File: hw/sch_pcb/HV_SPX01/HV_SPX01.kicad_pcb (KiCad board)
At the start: 2 copper layers, 21 x 23.1 mm, 37 parts, among them IC1 MAX1847EEE+, J1 Conn_01x01_Pin, J2 Conn_01x01_Pin, J3 Conn_01x01_Pin, J4 Conn_01x01_Pin, J5 Conn_01x01_Pin, J6 Conn_01x01_Pin, J7 Conn_01x01_Pin, Q1 PMOS

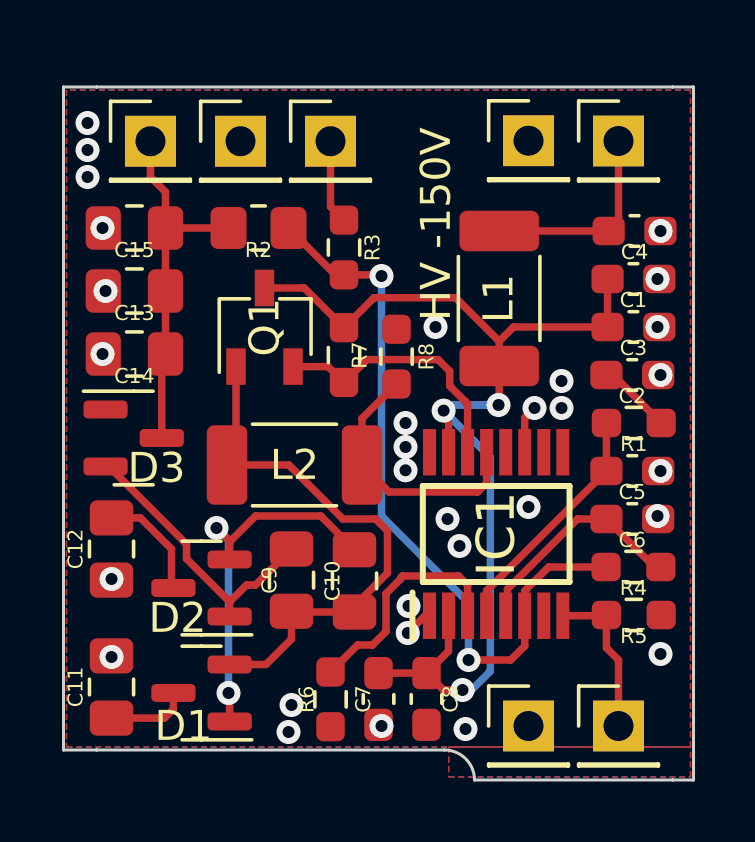
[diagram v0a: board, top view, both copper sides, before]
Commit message: conn footprint changed - courtyard was overlapping
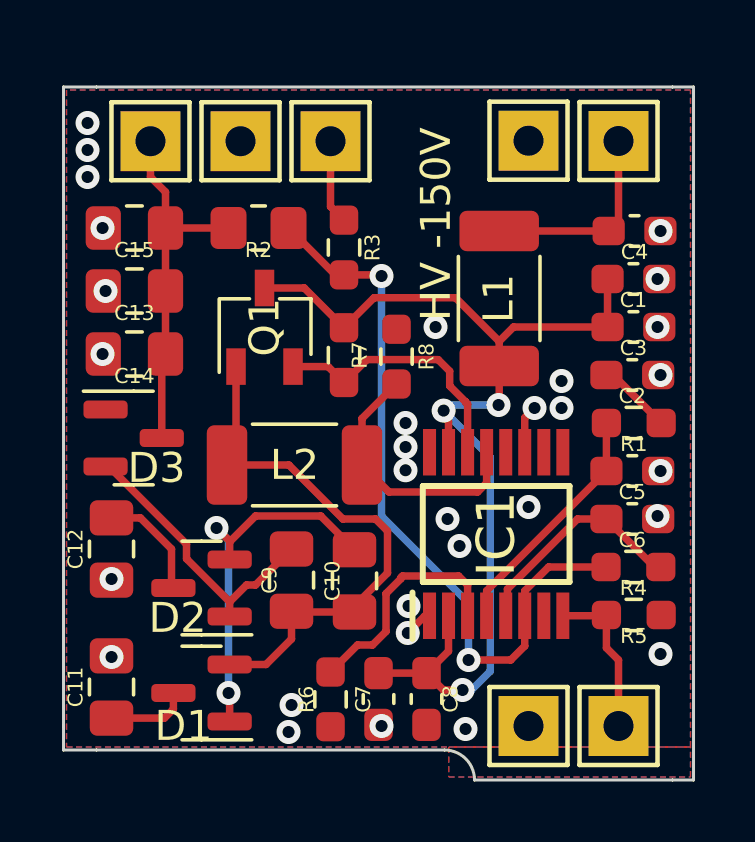
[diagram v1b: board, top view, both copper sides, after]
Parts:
- J1, J2, J3, J4, J5, J6, J7: footprint Connector_PinHeader_2.54mm:PinHeader_1x01_P2.54mm_Vertical -> Mlab_CON:1_kontakty
